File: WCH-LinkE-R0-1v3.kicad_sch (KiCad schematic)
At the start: 38 parts, among them Q1 DMG1012UW-7, Q2 DMG1012UW-7, SW1 16V 50mA, SW2 16V 50mA, SW3 16V 50mA, U3 CH32V305FBP6

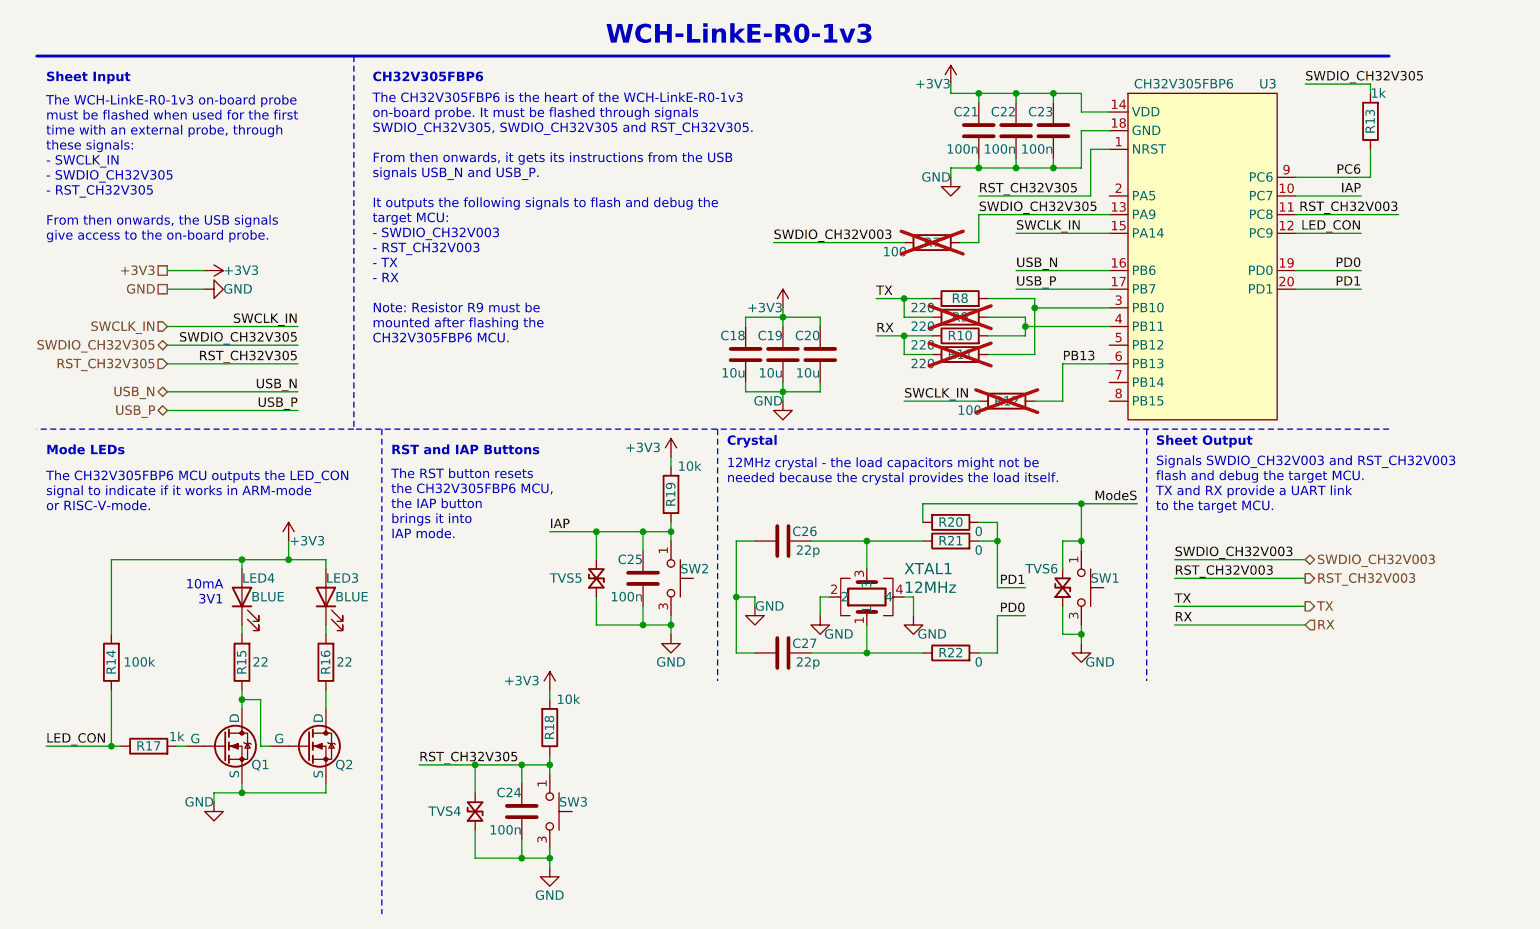
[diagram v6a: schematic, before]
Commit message: Rename net 'SWCLK_IN' into 'SWCLK_CH32V305'
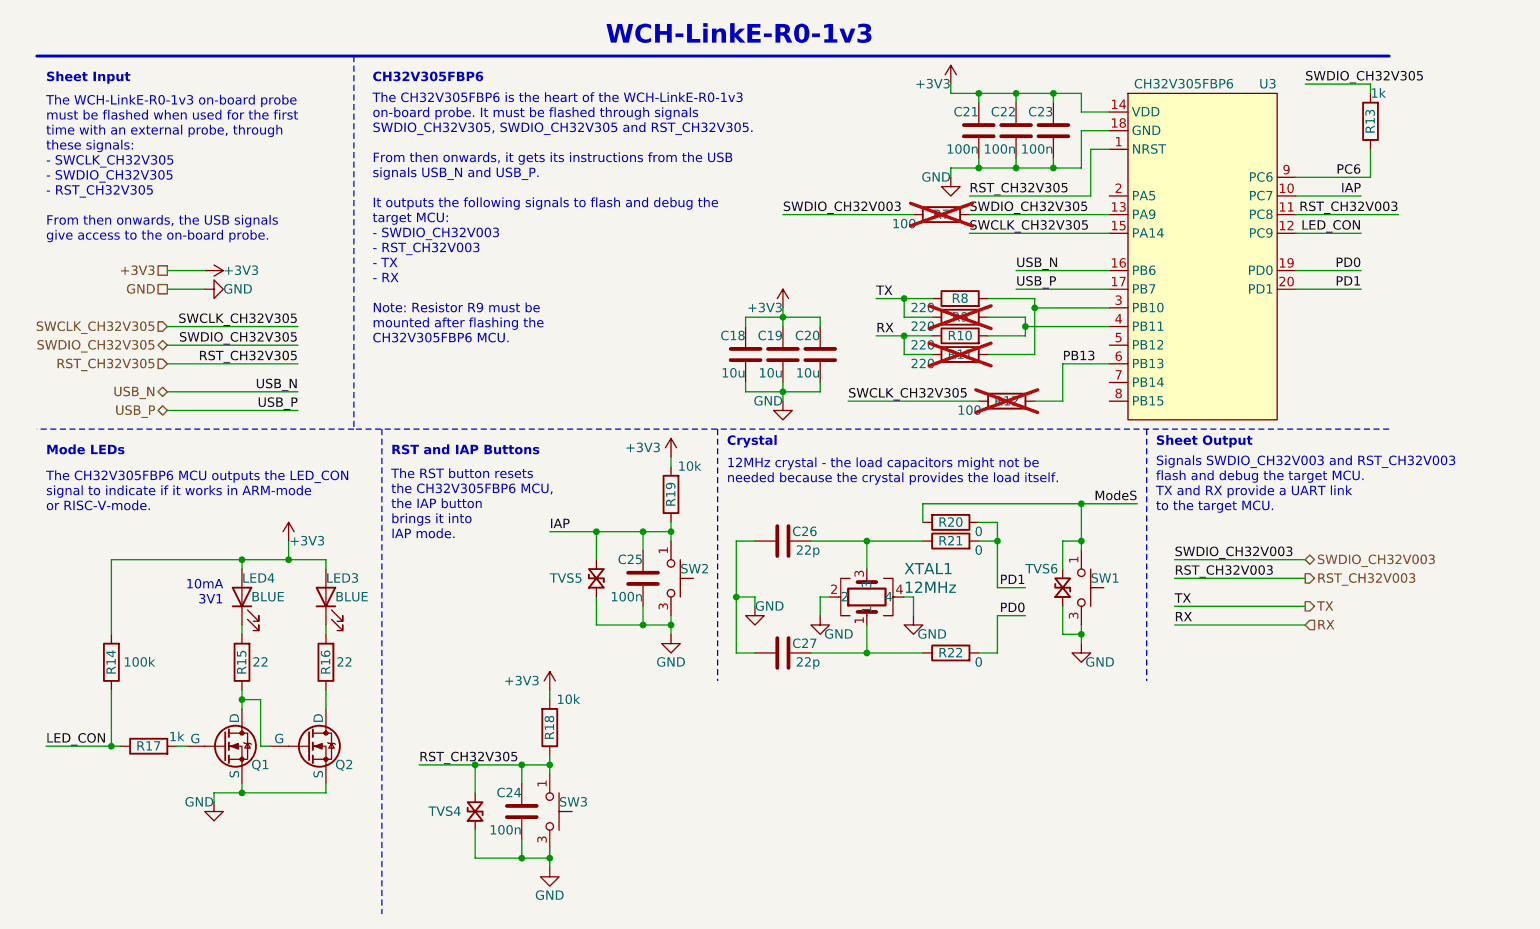
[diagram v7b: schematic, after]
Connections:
- net SWCLK_IN renamed SWCLK_CH32V305
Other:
- note added: "The WCH-LinkE-R0-1v3 on-board probe must be flashed when used for the first time with an external probe, through these signals: - SWCLK_CH32V305 - SWDIO_CH32V305 - RST_CH32V305 From then onwards, the USB signals give access to the on-board probe."
- note removed: "The WCH-LinkE-R0-1v3 on-board probe must be flashed when used for the first time with an external probe, through these signals: - SWCLK_IN - SWDIO_CH32V305 - RST_CH32V305 From then onwards, the USB signals give access to the on-board probe."
- moved on the sheet: R7
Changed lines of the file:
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@@
     (stroke (width 0) (type default))
   )
-  (wire (pts (xy 140.97 38.1) (xy 156.21 38.1))
+  (wire (pts (xy 139.7 38.1) (xy 156.21 38.1))
     (stroke (width 0) (type default))
   )
@@
     (stroke (width 0) (type default))
   )
-  (wire (pts (xy 140.97 40.64) (xy 158.75 40.64))
-    (stroke (width 0) (type default))
-  )
   (wire (pts (xy 125.73 100.33) (xy 125.73 96.52))
     (stroke (width 0) (type default))
@@
     (stroke (width 0) (type default))
   )
-  (wire (pts (xy 130.81 66.04) (xy 140.97 66.04))
+  (wire (pts (xy 123.19 66.04) (xy 140.97 66.04))
     (stroke (width 0) (type default))
   )
@@
     (stroke (width 0) (type default))
   )
-  (wire (pts (xy 138.43 44.45) (xy 140.97 44.45))
+  (wire (pts (xy 139.7 40.64) (xy 158.75 40.64))
     (stroke (width 0) (type default))
   )
@@
     (stroke (width 0) (type default))
   )
-  (wire (pts (xy 113.03 44.45) (xy 130.81 44.45))
+  (wire (pts (xy 114.3 40.64) (xy 132.08 40.64))
     (stroke (width 0) (type default))
   )
@@
     (stroke (width 0) (type default))
   )
-  (wire (pts (xy 146.05 43.18) (xy 158.75 43.18))
+  (wire (pts (xy 139.7 43.18) (xy 158.75 43.18))
     (stroke (width 0) (type default))
   )
@@
   )
   (wire (pts (xy 99.06 95.25) (xy 99.06 96.52))
-    (stroke (width 0) (type default))
-  )
-  (wire (pts (xy 140.97 44.45) (xy 140.97 40.64))
     (stroke (width 0) (type default))
   )
@@
     (effects (font (size 1.27 1.27)) (justify left bottom))
   )
-  (text "The WCH-LinkE-R0-1v3 on-board probe\nmust be flashed when used for the first\ntime with an external probe, through\nthese signals:\n- SWCLK_IN\n- SWDIO_CH32V305\n- RST_CH32V305\n\nFrom then onwards, the USB signals\ngive access to the on-board probe."
+  (text "The WCH-LinkE-R0-1v3 on-board probe\nmust be flashed when used for the first\ntime with an external probe, through\nthese signals:\n- SWCLK_CH32V305\n- SWDIO_CH32V305\n- RST_CH32V305\n\nFrom then onwards, the USB signals\ngive access to the on-board probe."
     (at 13.97 44.45 0)
     (effects (font (size 1.27 1.27)) (justify left bottom))
@@
     (effects (font (size 1.27 1.27)) (justify right bottom))
   )
-  (label "SWCLK_IN" (at 130.81 66.04 0) (fields_autoplaced)
+  (label "SWCLK_CH32V305" (at 123.19 66.04 0) (fields_autoplaced)
     (effects (font (size 1.27 1.27)) (justify left bottom))
   )
@@
     (effects (font (size 1.27 1.27)) (justify left bottom))
   )
-  (label "SWDIO_CH32V003" (at 113.03 44.45 0) (fields_autoplaced)
+  (label "SWDIO_CH32V003" (at 114.3 40.64 0) (fields_autoplaced)
     (effects (font (size 1.27 1.27)) (justify left bottom))
   )
@@
     (effects (font (size 1.27 1.27)) (justify right bottom))
   )
-  (label "RST_CH32V305" (at 140.97 38.1 0) (fields_autoplaced)
-    (effects (font (size 1.27 1.27)) (justify left bottom))
-  )
-  (label "SWCLK_IN" (at 146.05 43.18 0) (fields_autoplaced)
+  (label "RST_CH32V305" (at 139.7 38.1 0) (fields_autoplaced)
+    (effects (font (size 1.27 1.27)) (justify left bottom))
+  )
+  (label "SWCLK_CH32V305" (at 139.7 43.18 0) (fields_autoplaced)
     (effects (font (size 1.27 1.27)) (justify left bottom))
   )
@@
     (effects (font (size 1.27 1.27)) (justify right bottom))
   )
-  (label "SWDIO_CH32V305" (at 140.97 40.64 0) (fields_autoplaced)
+  (label "SWDIO_CH32V305" (at 139.7 40.64 0) (fields_autoplaced)
     (effects (font (size 1.27 1.27)) (justify left bottom))
   )
@@
     (effects (font (size 1.27 1.27)) (justify left bottom))
   )
-  (label "SWCLK_IN" (at 48.26 55.88 180) (fields_autoplaced)
+  (label "SWCLK_CH32V305" (at 48.26 55.88 180) (fields_autoplaced)
     (effects (font (size 1.27 1.27)) (justify right bottom))
   )
@@
     (effects (font (size 1.27 1.27)) (justify right))
   )
-  (hierarchical_label "SWCLK_IN" (shape input) (at 30.48 55.88 180) (fields_autoplaced)
+  (hierarchical_label "SWCLK_CH32V305" (shape input) (at 30.48 55.88 180) (fields_autoplaced)
     (effects (font (size 1.27 1.27)) (justify right))
   )
@@
     )
   )
-  (symbol (lib_id "Device:R") (at 134.62 44.45 90) (unit 1)
+  (symbol (lib_id "Device:R") (at 135.89 40.64 90) (unit 1)
     (in_bom no) (on_board yes) (dnp yes)
-    (property "Reference" "R7" (at 134.62 44.45 90)
-      (effects (font (size 1.27 1.27)))
-    )
-    (property "Value" "100" (at 129.54 45.72 90)
-      (effects (font (size 1.27 1.27)))
-    )
-    (property "Footprint" "Resistor_SMD:R_0402_1005Metric_Pad0.72x0.64mm_HandSolder" (at 134.62 46.228 90)
-      (effects (font (size 1.27 1.27)) hide)
-    )
-    (property "Datasheet" "~" (at 134.62 44.45 0)
-      (effects (font (size 1.27 1.27)) hide)
-    )
-    (property "Manufacturer" "UNI-ROYAL(Uniroyal Elec)" (at 134.62 44.45 0)
-      (effects (font (size 1.27 1.27)) hide)
-    )
-    (property "MPN" "0402WGF1000TCE" (at 134.62 44.45 90)
-      (effects (font (size 1.27 1.27)) hide)
-    )
-    (property "JLCPCB Part #" "C25076" (at 134.62 44.45 90)
-      (effects (font (size 1.27 1.27)) hide)
-    )
+    (property "Reference" "R7" (at 135.89 40.64 90)
+      (effects (font (size 1.27 1.27)))
+    )
+    (property "Value" "100" (at 130.81 41.91 90)
+      (effects (font (size 1.27 1.27)))
+    )
+    (property "Footprint" "Resistor_SMD:R_0402_1005Metric_Pad0.72x0.64mm_HandSolder" (at 135.89 42.418 90)
+      (effects (font (size 1.27 1.27)) hide)
+    )
+    (property "Datasheet" "~" (at 135.89 40.64 0)
+      (effects (font (size 1.27 1.27)) hide)
+    )
+    (property "Manufacturer" "UNI-ROYAL(Uniroyal Elec)" (at 135.89 40.64 0)
+      (effects (font (size 1.27 1.27)) hide)
+    )
+    (property "MPN" "0402WGF1000TCE" (at 135.89 40.64 90)
+      (effects (font (size 1.27 1.27)) hide)
+    )
+    (property "JLCPCB Part #" "C25076" (at 135.89 40.64 90)
+      (effects (font (size 1.27 1.27)) hide)
+    )

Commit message: Schematic cleanup
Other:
- note added: "->"
- note added: "<-"
- note added: "RST_CH32V003"
- note added: "RST_CH32V305"
- note added: "SWCLK_CH32V305"
- note added: "SWDIO_CH32V003"
- note added: "SWDIO_CH32V305"
- note added: "The CH32V305FBP6 is the heart of the WCH-LinkE-R0-1v3 on-board probe. It must be flashed through signals , and . From then onwards, it gets its instructions from the USB signals USB_N and USB_P. It outputs the following signals to flash and debug the target MCU: - - - TX - RX Note: Resistor R7 must be mounted after flashing the CH32V305FBP6 MCU."
- note added: "The WCH-LinkE-R0-1v3 on-board probe must be flashed when used for the first time with an external probe, through these signals: - - - From then onwards, the USB signals give access to the on-board probe."
- note removed: "The CH32V305FBP6 is the heart of the WCH-LinkE-R0-1v3 on-board probe. It must be flashed through signals SWDIO_CH32V305, SWDIO_CH32V305 and RST_CH32V305. From then onwards, it gets its instructions from the USB signals USB_N and USB_P. It outputs the following signals to flash and debug the target MCU: - SWDIO_CH32V003 - RST_CH32V003 - TX - RX Note: Resistor R9 must be mounted after flashing the 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"
- note removed: "The WCH-LinkE-R0-1v3 on-board probe must be flashed when used for the first time with an external probe, through these signals: - SWCLK_CH32V305 - SWDIO_CH32V305 - RST_CH32V305 From then onwards, the USB signals give access to the on-board probe."
- moved on the sheet: C18, C19, C20, C21, C22, C23, C24, C25, C26, C27, R10, R11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
